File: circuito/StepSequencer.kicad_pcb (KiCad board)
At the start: 2 copper layers, 147.8 x 117.1 mm, 81 parts, among them P1 BEAGLEBONE_BLACK, SW0 SW_PUSH, SW1 SW_PUSH, SW10 SW_PUSH, SW11 SW_PUSH, SW12 SW_PUSH, SW13 SW_PUSH, SW14 SW_PUSH, SW15 SW_PUSH, SW2 SW_PUSH, SW3 SW_PUSH, SW4 SW_PUSH, SW5 SW_PUSH, SW6 SW_PUSH, SW7 SW_PUSH, SW8 SW_PUSH, SW9 SW_PUSH

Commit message: PCB Casi listo
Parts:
- added ?: , StepSequencer:LOGO, F.Cu at (104.5, 48.0)
- added RV1: POT, StepSequencer:POT_AZUL, F.Cu at (136.7, 52.8)
- added RV2: POT, StepSequencer:POT_AZUL, F.Cu at (160.3, 52.8)
- D1_0, D1_1, D1_10, D1_11, D1_12, D1_13, D1_14, D1_15, D1_2, D1_3, D1_4, D1_5, D1_6, D1_7, D1_8, D1_9, D2_0, D2_1, D2_10, D2_11, D2_12, D2_13, D2_14, D2_15, D2_2, D2_3, D2_4, D2_5, D2_6, D2_7, D2_8, D2_9: footprint LEDs:LED-5MM -> LEDs:LED-3MM
- SW0, SW1, SW10, SW11, SW12, SW13, SW14, SW15, SW2, SW3, SW4, SW5, SW6, SW7, SW8, SW9: footprint Buttons_Switches_ThroughHole:SW_PUSH-12mm -> StepSequencer:BOTON
- moved P1 86.8 mm to (68.8, 92.2)
- moved D1_0 58.6 mm to (96.5, 126.0)
- moved D1_8 58.6 mm to (96.5, 85.1)
- moved D2_0 58.6 mm to (96.5, 104.5)
- moved D2_8 58.6 mm to (96.5, 63.7)
- moved R2_8 58.6 mm to (97.6, 58.6)
- moved R1_0 58.6 mm to (97.8, 130.8)
- moved R2_0 58.6 mm to (97.8, 99.5)
- moved SW8 58.6 mm to (97.8, 74.4), turned to 0 degrees
- moved SW0 58.6 mm to (97.8, 115.3), turned to 0 degrees
- moved SW1 57.9 mm to (112.0, 115.3), turned to 0 degrees
- moved D1_1 57.6 mm to (111.0, 126.0)
- moved D2_1 57.6 mm to (111.0, 104.5)
- moved R2_1 57.6 mm to (112.3, 99.5)
- moved SW9 57.6 mm to (112.3, 74.4), turned to 0 degrees
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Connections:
- P1 pad B34: GNDA -> GNDD
- P1 pad B37: (no net) -> /pot0
- P1 pad B39: (no net) -> /pot1
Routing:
- net GNDD: track 623.7 -> 700.0 mm, vias 0 -> 4
- net +1V8: track 0.00 -> 74.3 mm, vias 0 -> 1
- net /pot1: track 0.00 -> 54.3 mm, vias 0 -> 4
- net /pot0: track 0.00 -> 43.6 mm, vias 0 -> 1
- net /led2_15: track 95.9 -> 137.1 mm, vias 3 -> 1
- net /btn15: track 85.0 -> 123.9 mm, vias 3 -> 5
- net /led1_7: track 44.9 -> 82.7 mm
- net /led1_15: track 61.4 -> 98.5 mm, vias 5 -> 4
- net /led2_5: track 53.0 -> 87.9 mm, vias 1 -> 3
- net /led1_5: track 18.3 -> 50.4 mm
- net /led1_4: track 14.3 -> 44.3 mm
- net /led1_12: track 7.06 -> 37.1 mm
- net /led2_6: track 53.6 -> 82.9 mm, vias 3 -> 5
- net /btn7: track 50.6 -> 77.6 mm, vias 1 -> 3
- net /led1_11: track 5.19 -> 31.7 mm
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- added copper zone on B.Cu, net GNDD
- added copper zone on F.Cu, net GNDD
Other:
- board size 147.8 x 117.1 mm -> 126.5 x 115 mm
- net class Default: via_dia 0.6 -> 0.8

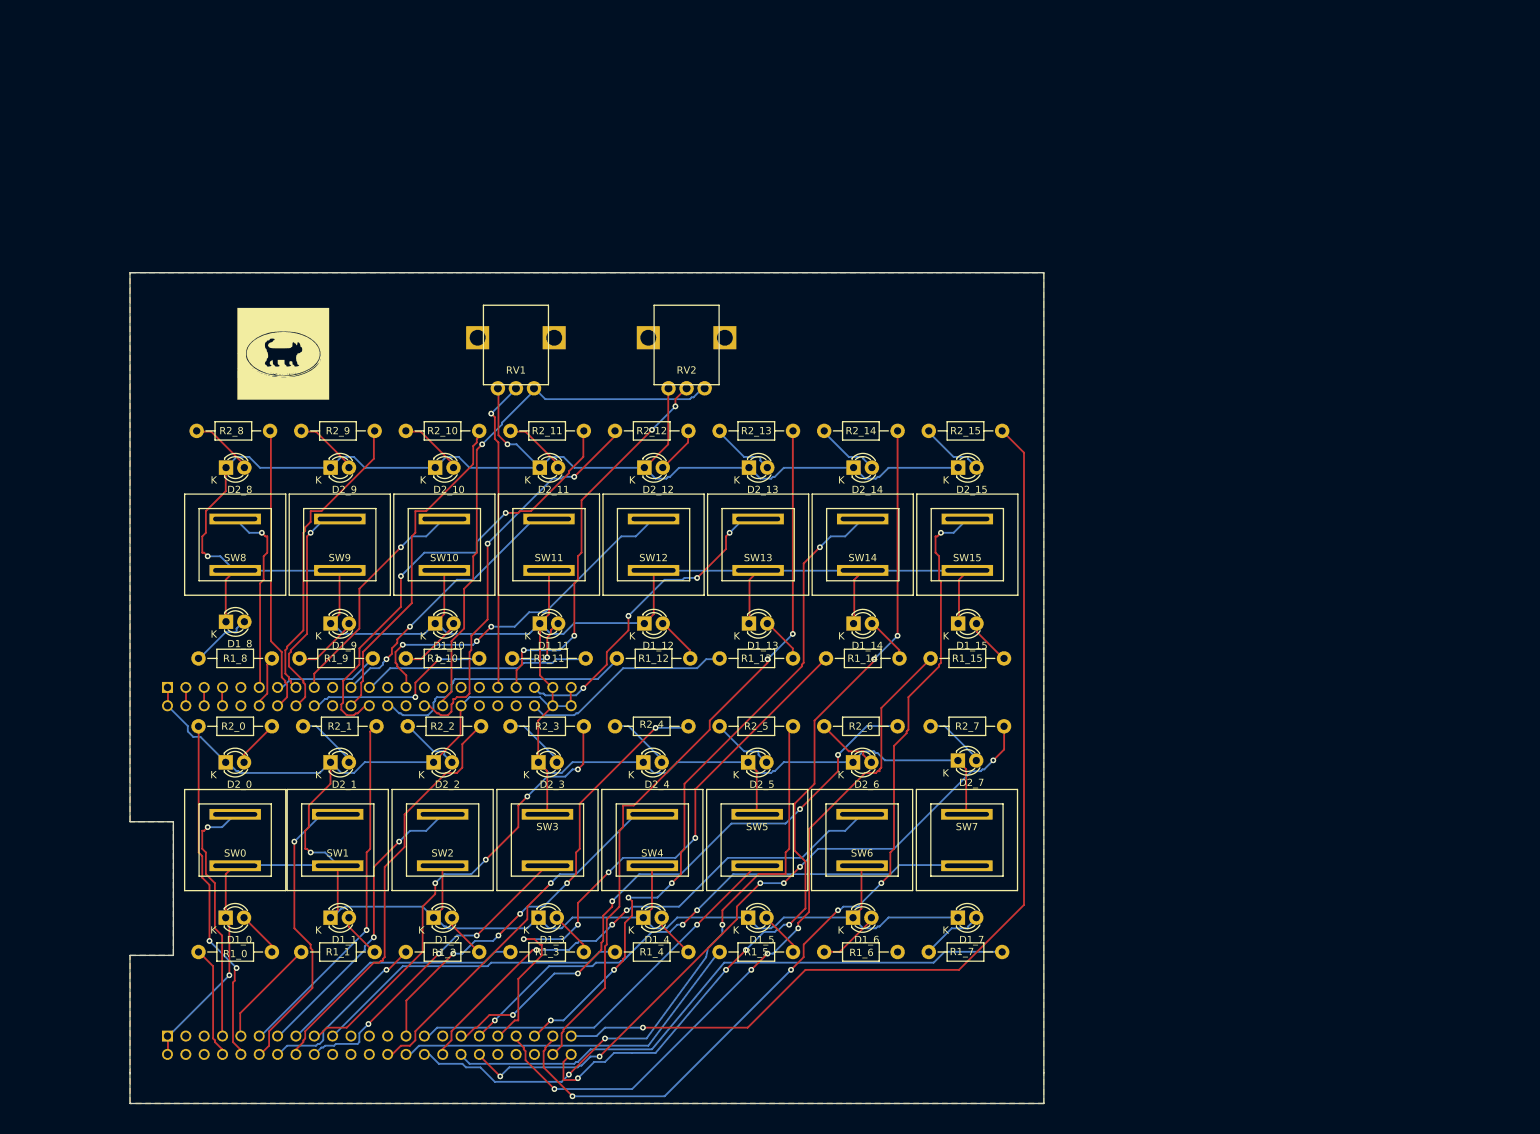
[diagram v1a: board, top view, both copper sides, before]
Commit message: se genero u pad de tornillo 1/4, se dejo con la opcion pad para tornillos propuesta por la comunidad, no se han podido conectar a gnd
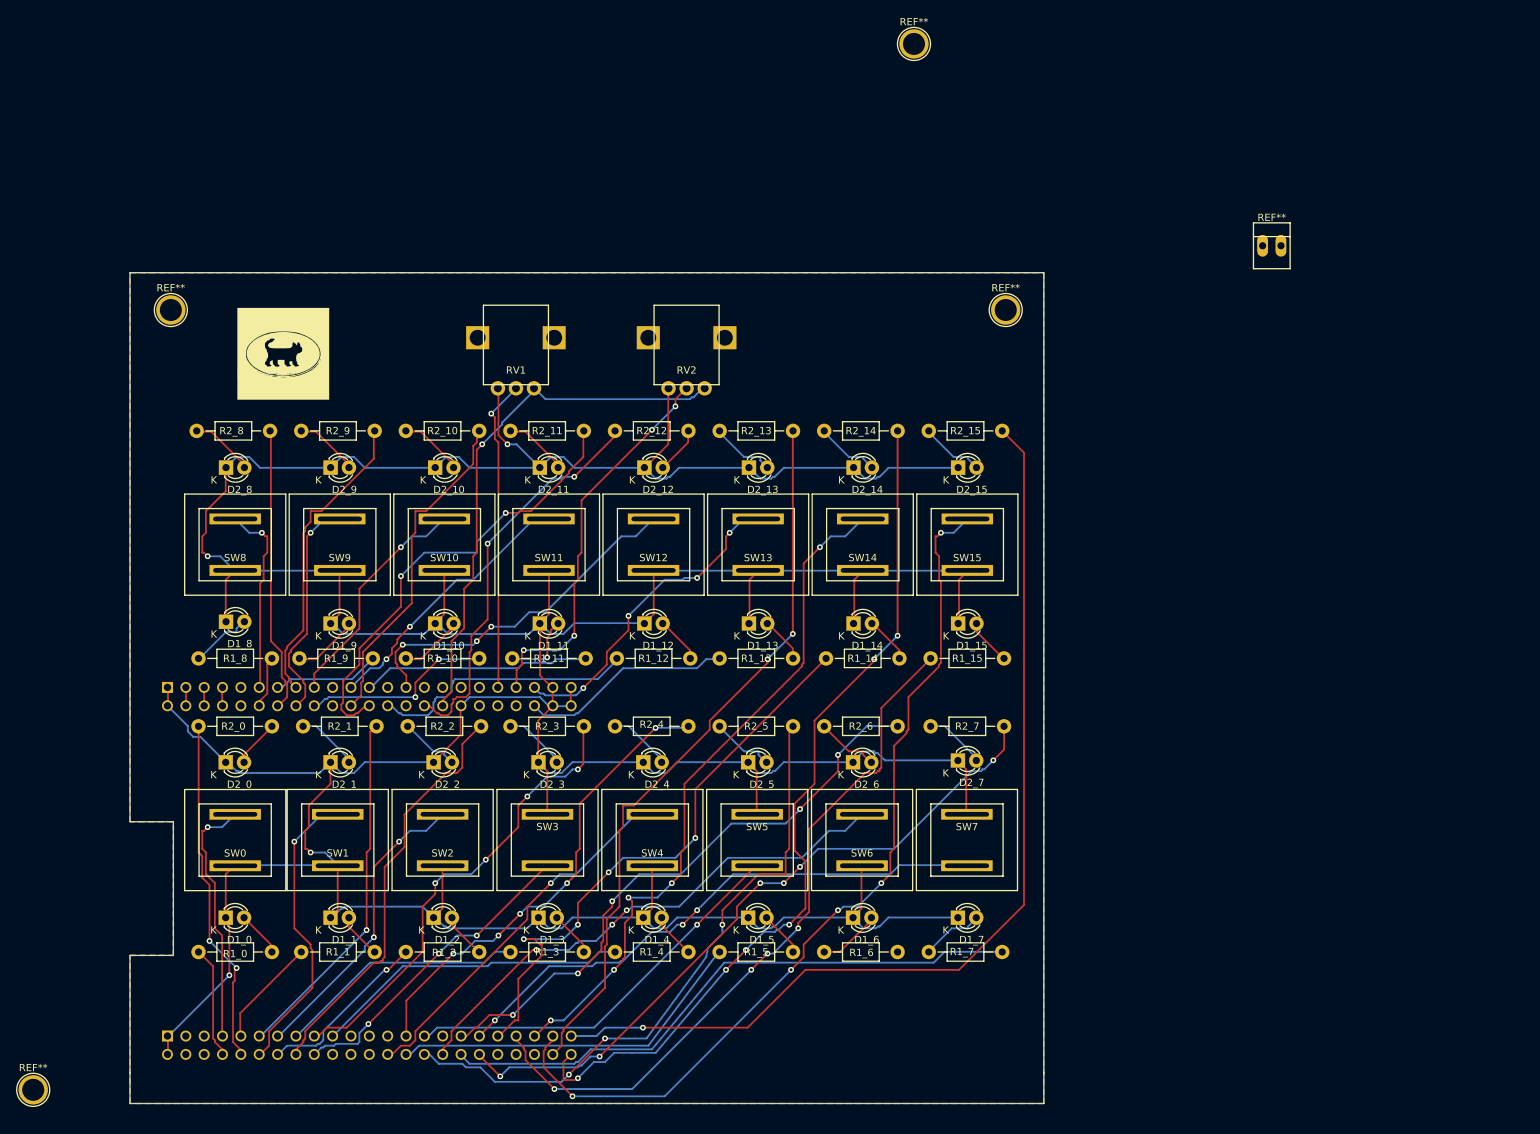
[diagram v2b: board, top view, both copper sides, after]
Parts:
- added REF**: PINHEAD1-2, Connect:PINHEAD1-2, F.Cu at (241.3, 33.0)
- added REF**: 1pin, Connect:1pin, F.Cu at (204.5, 41.9)
- added REF**: 1pin, Connect:1pin, F.Cu at (88.9, 41.9)
- added REF**: 1pin, Connect:1pin, F.Cu at (69.8, 149.9)
- added REF**: 1pin, Connect:1pin, F.Cu at (191.8, 5.08)
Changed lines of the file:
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@@
-(kicad_pcb (version 4) (host pcbnew 0.201508280901+6131~28~ubuntu14.04.1-product)
+(kicad_pcb (version 4) (host pcbnew 0.201510010346+6232~30~ubuntu14.04.1-product)
   (general
     (links 144)
     (no_connects 0)
-    (area 115.75 13.75 261.5 144.5)
+    (area 63.5 27.94 246.38 163.83)
     (thickness 1.6)
     (drawings 16)
     (tracks 1352)
     (zones 0)
-    (modules 84)
+    (modules 89)
     (nets 87)
   )
@@
     (last_trace_width 0.25)
     (trace_clearance 0.2)
-    (zone_clearance 0.4)
+    (zone_clearance 0.508)
     (zone_45_only no)
     (trace_min 0.2)
@@
     (mod_text_size 1 1)
     (mod_text_width 0.15)
-    (pad_size 1.524 1.524)
-    (pad_drill 0.762)
+    (pad_size 9 9)
+    (pad_drill 6.36)
     (pad_to_mask_clearance 0.2)
     (aux_axis_origin 0 0)
@@
       (xy -1.730136 -2.845029) (xy -0.823814 -2.988357) (xy 0.082926 -3.031102) (xy 0.970884 -2.977914)) (layer F.SilkS) (width 0.01))
   )
+  (module Connect:PINHEAD1-2 (layer F.Cu)
+    (at 241.3 33.02)
+    (attr virtual)
+    (fp_text reference REF** (at 0 -3.9) (layer F.SilkS)
+      (effects (font (size 1 1) (thickness 0.15)))
+    )
+    (fp_text value PINHEAD1-2 (at 0 3.81) (layer F.Fab)
+      (effects (font (size 1 1) (thickness 0.15)))
+    )
+    (fp_line (start 2.54 -1.27) (end -2.54 -1.27) (layer F.SilkS) (width 0.15))
+    (fp_line (start 2.54 3.175) (end -2.54 3.175) (layer F.SilkS) (width 0.15))
+    (fp_line (start -2.54 -3.175) (end 2.54 -3.175) (layer F.SilkS) (width 0.15))
+    (fp_line (start -2.54 -3.175) (end -2.54 3.175) (layer F.SilkS) (width 0.15))
+    (fp_line (start 2.54 -3.175) (end 2.54 3.175) (layer F.SilkS) (width 0.15))
+    (pad 1 thru_hole oval (at -1.27 0) (size 1.50622 3.01498) (drill 0.99822) (layers *.Cu *.Mask))
+    (pad 2 thru_hole oval (at 1.27 0) (size 1.50622 3.01498) (drill 0.99822) (layers *.Cu *.Mask))
+  )
+  (module Connect:1pin (layer F.Cu)
+    (at 204.47 41.91)
+    (descr "module 1 pin (ou trou mecanique de percage)")
+    (tags DEV)
+    (fp_text reference REF** (at 0 -3.048) (layer F.SilkS)
+      (effects (font (size 1 1) (thickness 0.15)))
+    )
+    (fp_text value 1pin (at 0 2.794) (layer F.Fab)
+      (effects (font (size 1 1) (thickness 0.15)))
+    )
+    (fp_circle (center 0 0) (end 0 -2.286) (layer F.SilkS) (width 0.15))
+    (pad 1 thru_hole circle (at 0 0) (size 4.064 4.064) (drill 3.048) (layers *.Cu *.Mask F.SilkS))
+  )
+  (module Connect:1pin (layer F.Cu)
+    (at 88.9 41.91)
+    (descr "module 1 pin (ou trou mecanique de percage)")
+    (tags DEV)
+    (fp_text reference REF** (at 0 -3.048) (layer F.SilkS)
+      (effects (font (size 1 1) (thickness 0.15)))
+    )
+    (fp_text value 1pin (at 0 2.794) (layer F.Fab)
+      (effects (font (size 1 1) (thickness 0.15)))
+    )
+    (fp_circle (center 0 0) (end 0 -2.286) (layer F.SilkS) (width 0.15))
+    (pad 1 thru_hole circle (at 0 0) (size 4.064 4.064) (drill 3.048) (layers *.Cu *.Mask F.SilkS))
+  )
+  (module Connect:1pin (layer F.Cu)
+    (at 69.85 149.86)
+    (descr "module 1 pin (ou trou mecanique de percage)")
+    (tags DEV)
+    (fp_text reference REF** (at 0 -3.048) (layer F.SilkS)
+      (effects (font (size 1 1) (thickness 0.15)))
+    )
+    (fp_text value 1pin (at 0 2.794) (layer F.Fab)
+      (effects (font (size 1 1) (thickness 0.15)))
+    )
+    (fp_circle (center 0 0) (end 0 -2.286) (layer F.SilkS) (width 0.15))
+    (pad 1 thru_hole circle (at 0 0) (size 4.064 4.064) (drill 3.048) (layers *.Cu *.Mask F.SilkS))
+  )
+  (module Connect:1pin (layer F.Cu)
+    (at 191.77 5.08)
+    (descr "module 1 pin (ou trou mecanique de percage)")
+    (tags DEV)
+    (fp_text reference REF** (at 0 -3.048) (layer F.SilkS)
+      (effects (font (size 1 1) (thickness 0.15)))
+    )
+    (fp_text value 1pin (at 0 2.794) (layer F.Fab)
+      (effects (font (size 1 1) (thickness 0.15)))
+    )
+    (fp_circle (center 0 0) (end 0 -2.286) (layer F.SilkS) (width 0.15))
+    (pad 1 thru_hole circle (at 0 0) (size 4.064 4.064) (drill 3.048) (layers *.Cu *.Mask F.SilkS))
+  )
   (dimension 122.75 (width 0.3) (layer Cmts.User)

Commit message: Gato, gerber
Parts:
- removed ?: , StepSequencer:LOGO
- removed REF**: PINHEAD1-2, Connect:PINHEAD1-2
- removed REF** (x4): 1pin, Connect:1pin
- added G***: LOGO, StepSequencer:GATO3, F.Cu at (184.6, 135.2)
- added G***: LOGO, StepSequencer:GATO2, F.Cu at (139.2, 84.8)
- added P2: CONN_01X01, StepSequencer:SCREWS, F.Cu at (205.0, 150.0)
- added P3: CONN_01X01, StepSequencer:SCREWS, F.Cu at (205.0, 41.0)
- added P4: CONN_01X01, StepSequencer:SCREWS, F.Cu at (88.0, 150.0)
- added P5: CONN_01X01, StepSequencer:SCREWS, F.Cu at (88.0, 41.0)
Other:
- board size 126.5 x 115 mm -> 126.5 x 117.1 mm
